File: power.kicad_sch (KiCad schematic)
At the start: 73 parts, among them CON2 BARREL_JACK, U17 LMR51420, U18 LMR51420, U19 LMR51420, U20 LP5907-3.0, U21 LP2985A-10DBVR, U22 LD3920, U23 LD3920, U24 LD3920, U25 BU33SD5WG

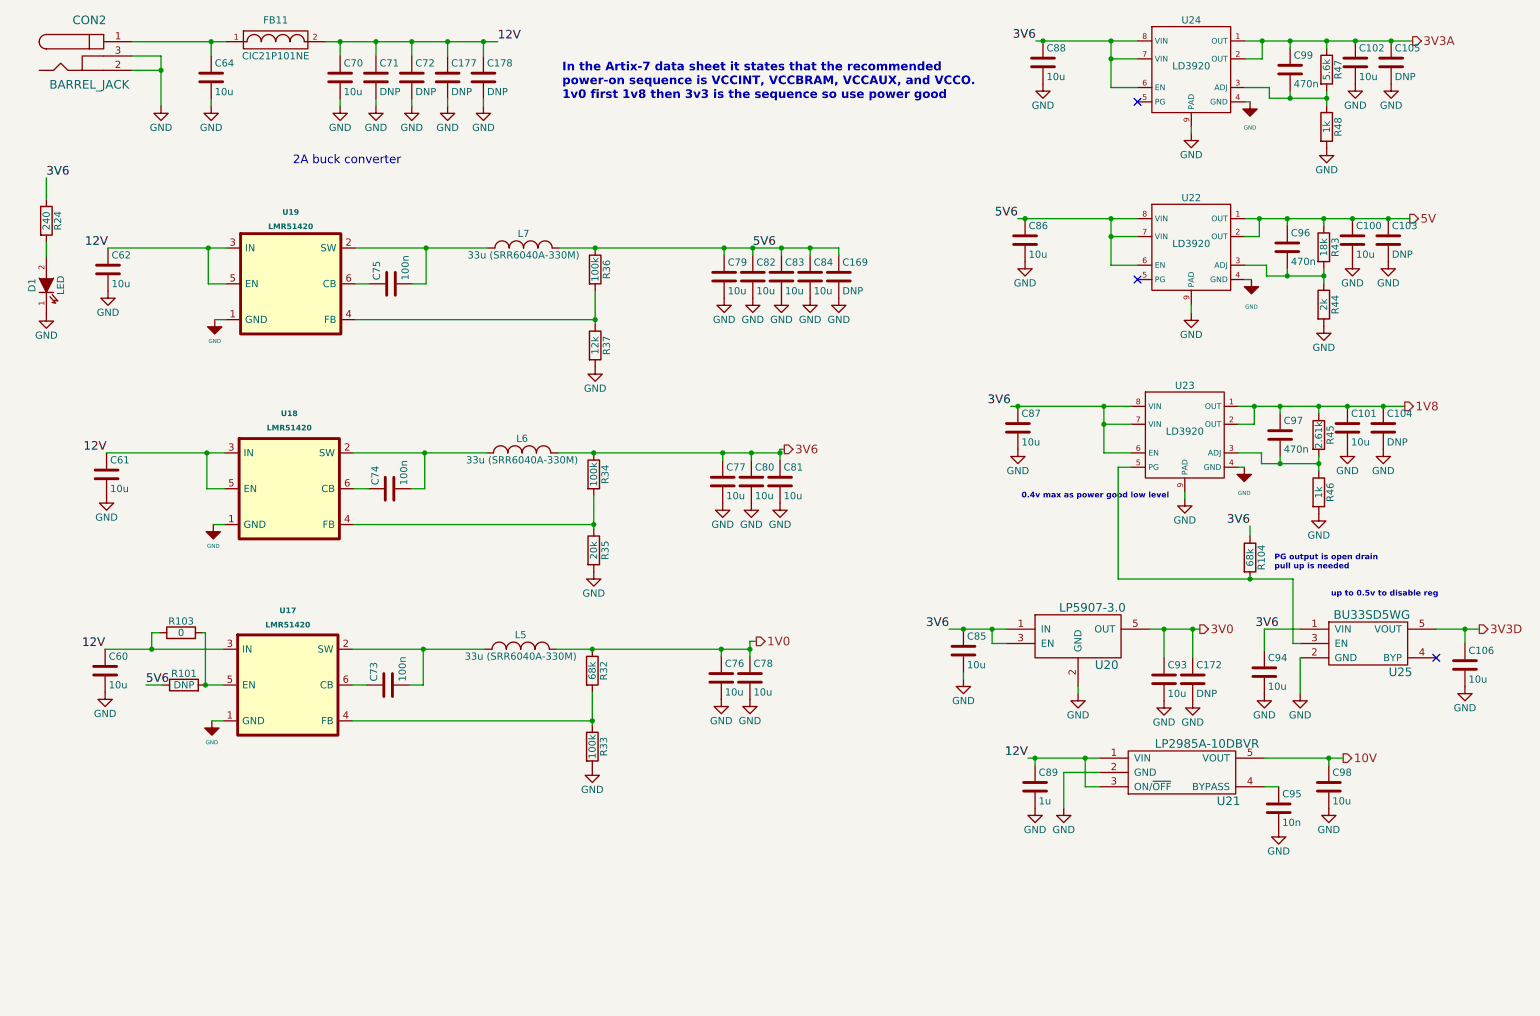
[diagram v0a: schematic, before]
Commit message: Leds are added to schematic netlist is generated will be placed on pcb
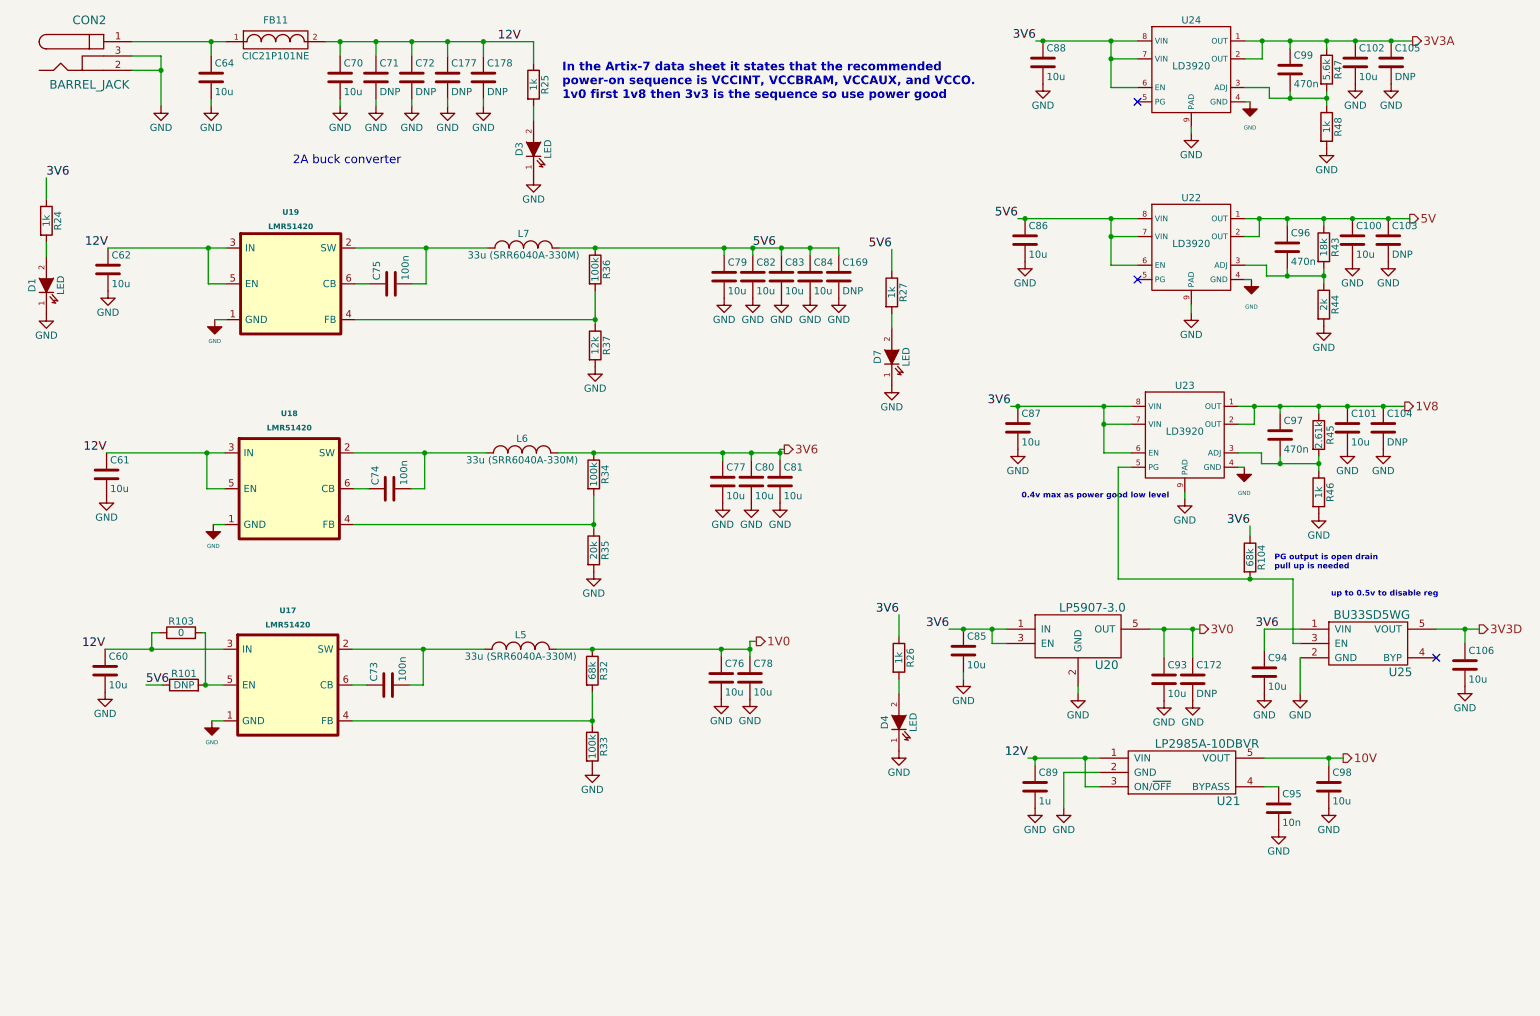
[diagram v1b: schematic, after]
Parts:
- added D3, D4, D7: LED, Footprints:Diode_0603, symbol fmcw3-rescue:LED
- added R25, R26, R27: 1k, Footprints:SMD_0402, symbol fmcw3-rescue:R
- R24: value 240 -> 1k
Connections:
- net 12V: now also R25.1
- net 3V6: now also R26.1
- net 5V6: now also R27.1
- net GND: now also D3.1 (K), D4.1 (K), D7.1 (K)
- new net: D7.2 (A), R27.2
- new net: D3.2 (A), R25.2
- new net: D4.2 (A), R26.2

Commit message: component name correction
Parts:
- FB11: value CIC21P101NE -> MPZ2012S101AT000
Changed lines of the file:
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@@
 			)
 		)
-		(property "Value" "CIC21P101NE"
+		(property "Value" "MPZ2012S101AT000"
 			(at 62.23 24.13 0)
 			(effects

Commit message: final corrections is done. Working!
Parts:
- R35: value 20k -> 18.7K
- R45: value 2.61k -> 49.9k
- R46: value 1k -> 18.7k
- R47: value 5.6k -> 18.7k
- R48: value 1k -> 3.3k
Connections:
- net 3V6: no longer C77.1, C80.1, C81.1, C85.1, C87.1, C88.1, C94.1, L6.2, R104.1, R26.1, R34.1, U20.1 (IN), U20.3 (EN), U23.6 (EN), U23.7 (VIN), U23.8 (VIN), U24.6 (EN), U24.7 (VIN), U24.8 (VIN), U25.1 (VIN)
- new net 3V8: C77.1, C80.1, C81.1, C85.1, C87.1, C88.1, C94.1, L6.2, R104.1, R26.1, R34.1, U20.1 (IN), U20.3 (EN), U23.6 (EN), U23.7 (VIN), U23.8 (VIN), U24.6 (EN), U24.7 (VIN), U24.8 (VIN), U25.1 (VIN)
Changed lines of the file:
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@@
 		)
 	)
-	(label "3V6"
+	(label "3V8"
 		(at 240.03 125.73 180)
 		(effects
@@
 		)
 	)
-	(label "3V6"
+	(label "3V8"
 		(at 192.532 86.233 180)
 		(effects
@@
 		)
 	)
-	(label "3V6"
+	(label "3V8"
 		(at 234.95 107.442 180)
 		(effects
@@
 		)
 	)
-	(label "3V6"
+	(label "3V8"
 		(at 181.61 125.73 180)
 		(effects
@@
 		)
 	)
-	(label "3V6"
+	(label "3V8"
 		(at 196.977 21.463 180)
 		(effects
@@
 		)
 	)
-	(label "3V6"
+	(label "3V8"
 		(at 172.72 123.19 180)
 		(effects
@@
 		)
 	)
-	(hierarchical_label "3V6"
+	(hierarchical_label "3V8"
 		(shape output)
 		(at 152.4 93.853 0)
@@
 			)
 		)
-		(property "Value" "5.6k"
+		(property "Value" "18.7k"
 			(at 248.539 26.543 90)
 			(effects
@@
 			)
 		)
-		(property "Value" "1k"
+		(property "Value" "3.3k"
 			(at 248.539 36.703 90)
 			(effects
@@
 			)
 		)
-		(property "Value" "2.61k"
+		(property "Value" "49.9k"
 			(at 247.142 91.313 90)
 			(effects
@@
 			)
 		)
-		(property "Value" "1k"
+		(property "Value" "18.7k"
 			(at 247.142 101.473 90)
 			(effects
@@
 			)
 		)
-		(property "Value" "20k"
+		(property "Value" "18.7K"
 			(at 118.618 111.76 90)
 			(effects

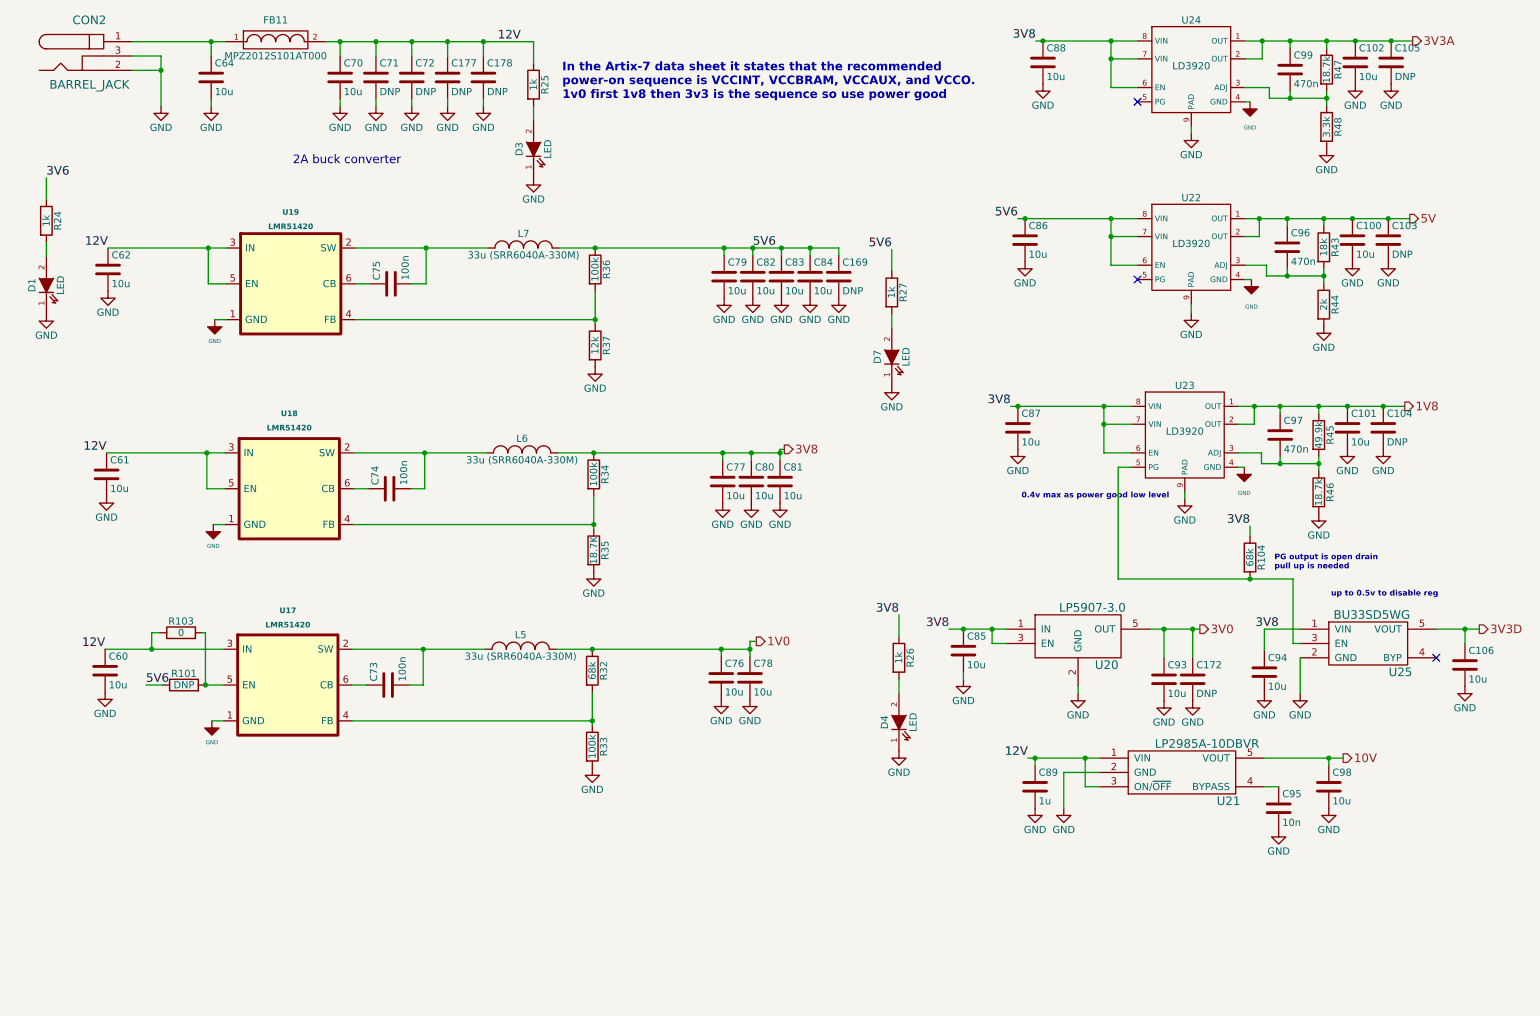
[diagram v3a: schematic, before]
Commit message: I increased the gap between voltage pours and also corrected signals cutting copper pour. Also not connected gnd occured in some layers are corrected with no copper zoens
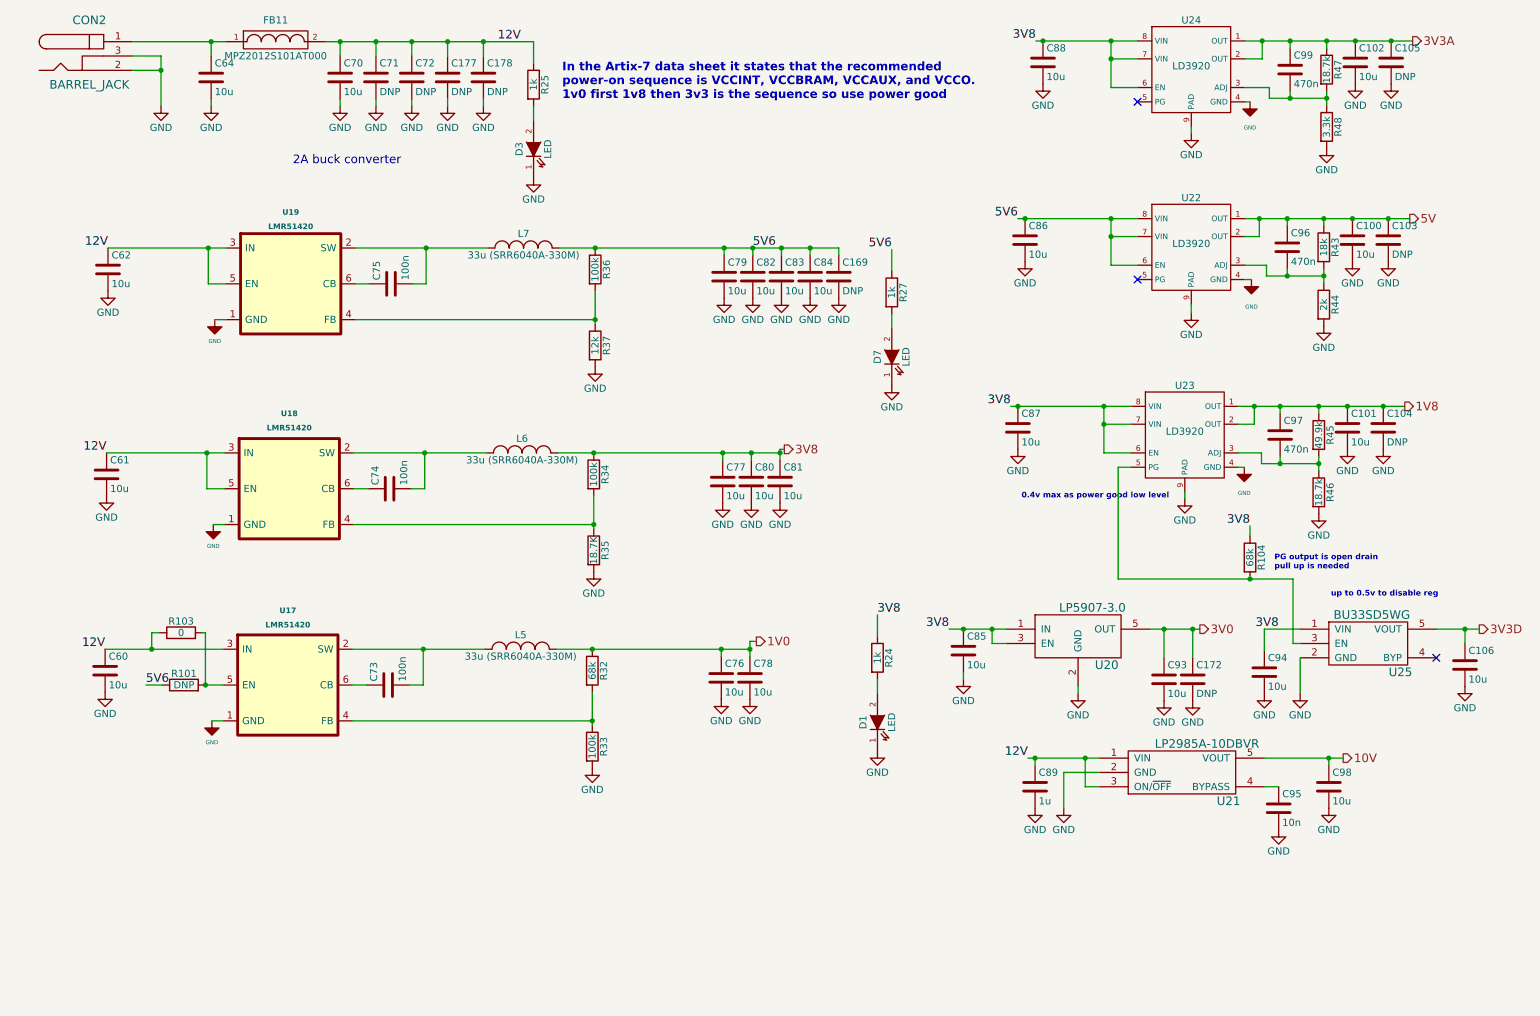
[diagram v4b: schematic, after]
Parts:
- removed D4: LED, Footprints:Diode_0603, symbol fmcw3-rescue:LED
- removed R26: 1k, Footprints:SMD_0402, symbol fmcw3-rescue:R
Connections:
- net 3V6 is gone; now on net 3V8: R24.1
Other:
- moved on the sheet: D1, R24

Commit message: hardware changes
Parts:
- added P5, P7, P8: CONN_01X01, fmcw3:MountingHole_3.2mm_M3_Pad_Via_mod, symbol fmcw3-rescue:CONN_01X01
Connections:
- net GND: now also P5.1 (P1), P7.1 (P1), P8.1 (P1)

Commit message: schematic is updated pcb is almost done
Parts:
- R104: value 68k -> 10k
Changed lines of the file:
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@@
 			)
 		)
-		(property "Value" "68k"
+		(property "Value" "10k"
 			(at 234.95 113.03 90)
 			(effects

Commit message: checks are done.
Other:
- moved on the sheet: C101, C104, C106, C172, C85, C87, C89, C93, C94, C95, C97, C98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

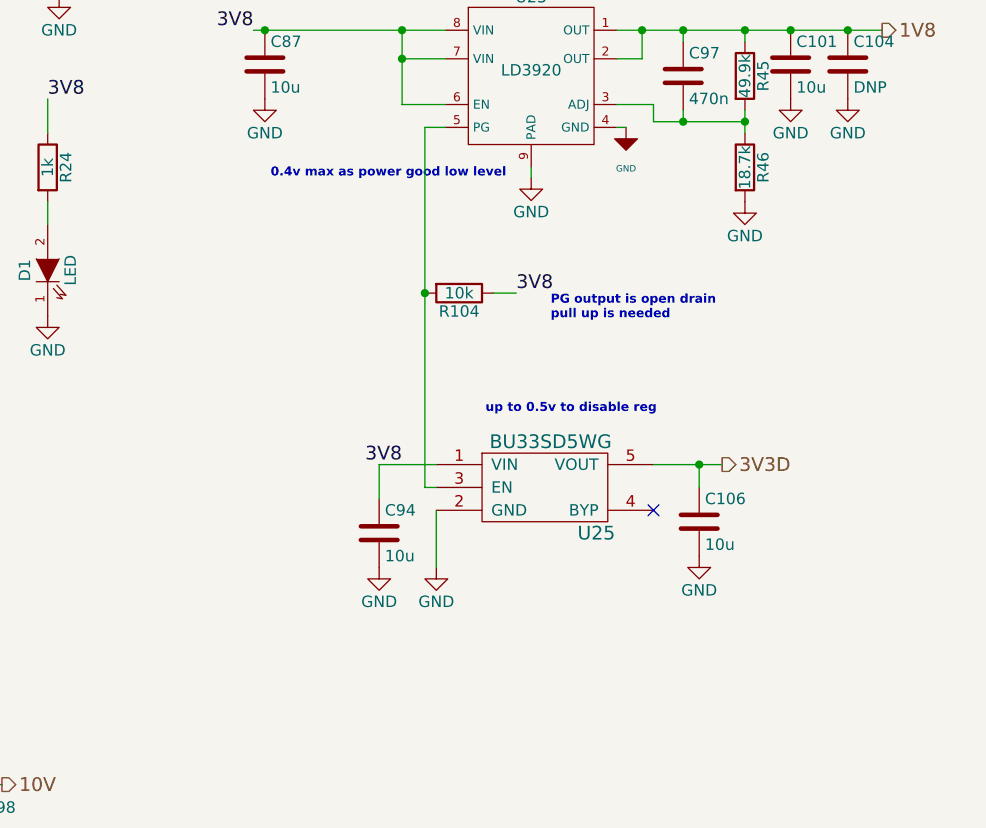
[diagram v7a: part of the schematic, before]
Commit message: 3.3v regulator is upgraded
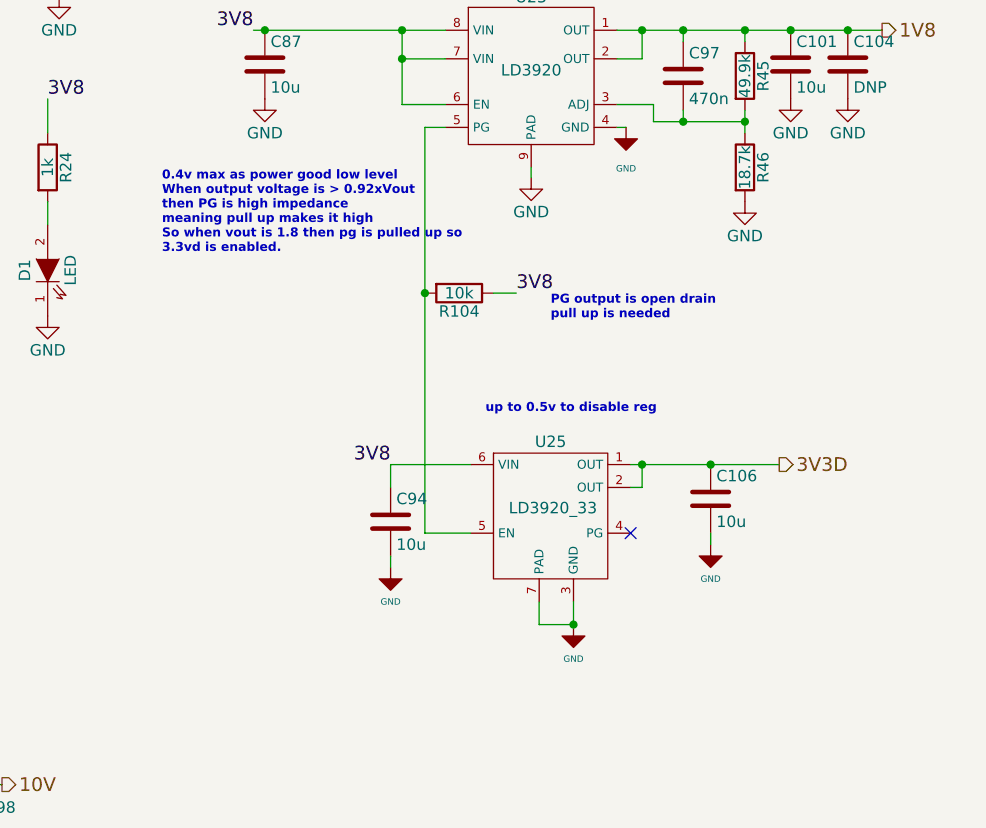
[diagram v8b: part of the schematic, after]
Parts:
- removed U25: BU33SD5WG, fmcw3:SOT-23-5, symbol fmcw3:MIC5301
- added U25: LD3920_33, Package_DFN_QFN:DFN-6-1EP_3x3mm_P0.95mm_EP1.7x2.6mm, symbol ld3920_33:LD3920_33
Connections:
- net 3V3D: now also U25.1 (OUT), U25.2 (OUT)
- net 3V8: now also U25.6 (VIN)
- net GND: now also U25.3 (GND), U25.7 (PAD)
- net at R104.2, U23.5 (PG): now also U25.5 (EN)
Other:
- note added: "0.4v max as power good low level When output voltage is > 0.92xVout then PG is high impedance meaning pull up makes it high So when vout is 1.8 then pg is pulled up so 3.3vd is enabled."
- note removed: "0.4v max as power good low level"
- moved on the sheet: C106, C94
